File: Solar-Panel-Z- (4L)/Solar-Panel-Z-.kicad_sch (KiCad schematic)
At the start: 80 parts, among them J1 FTS-105-01-L-DV-A, J2 U.FL-R-SMT-1, Q1 BSS138DWQ-7, Q2 MBT2222ADW1T1, Q3 BSS138DWQ-7, Q4 MBT2222ADW1T1, Q5 IRLML2803, U1 BQ25570RGRR, U2 TSL2561, U3 ATB2012-50011-T000, U4 NDS8434

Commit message: Changed design to TSL2691 and IRF7404 on Z- (4L)
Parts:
- removed R1, R2: 0, Resistor_SMD:R_0402_1005Metric, symbol Device:R_US
- removed U2: TSL2561, solarpanels:TSL2561, symbol solarpanels:symbols_TSL2561
- removed U4: NDS8434, solarpanels:NDS8434, symbol solarpanels:symbols_NDS8434
- added U2: TSL2591, solarpanels:TSL2591, symbol solarpanels:symbols_TSL2591
- added U4: IRF7404, Package_SO:SOIC-8_3.9x4.9mm_P1.27mm, symbol Transistor_FET:IRF7404
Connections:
- net +3V3: now also U2.5 (VDD)
- net BATT_P: now also U4.1 (S), U4.2 (S), U4.3 (S)
- net GND: now also U2.3 (GND)
- net SCL_LS: now also U2.1 (SCL)
- net SDA_LS: now also U2.6 (SDA)
- net VBURN: now also U4.5 (D), U4.6 (D), U4.7 (D), U4.8 (D)
- net at R10.2, R5.2, R7.2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: now also R5.1, R6.2, U1.7 (VBAT_OV)
- net at Q5.3 (D), R33.1: now also U4.4 (G)
- no-connect marks 1 -> 2
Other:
- moved on the sheet: C1, C2, C3, C6, D1, D5, H1, H2, H3, H4, H5, H6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

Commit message: Changed TSL2591 to BH1750
All boards (4L) except -Y
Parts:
- removed U2: TSL2591, solarpanels:TSL2591, symbol solarpanels:symbols_TSL2591
- added R1, R2: 0, Resistor_SMD:R_0402_1005Metric, symbol Device:R_US
- added U2: BH1750FVI-TR, WSOF6, symbol solarpanels:BH1750FVI-TR
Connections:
- net +3V3: now also R1.2, U2.1 (VCC)
- net GND: now also R2.1, U2.3 (GND)
- net SCL_LS: now also U2.6 (SCL)
- net SDA_LS: now also U2.4 (SDA)
- new net: R1.1, R2.2, U2.2 (ADDR)
- no-connect marks 2 -> 1
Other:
- moved on the sheet: C1

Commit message: Updated light sensor to OPT 3001, Updated solar diodes.
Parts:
- removed C12, C13: 10nF, Capacitor_SMD:C_0603_1608Metric, symbol Device:C
- removed D5: MSS1P4-M3_89A, solarpanels:MICROSMP, symbol Device:D_Schottky
- removed Q1, Q3: BSS138DWQ-7, Package_TO_SOT_SMD:SOT-363_SC-70-6, symbol mainboard:BSS138DWQ-7
- removed Q2, Q4: MBT2222ADW1T1, Package_TO_SOT_SMD:SOT-363_SC-70-6, symbol Transistor_BJT:MBT2222ADW1T1
- removed R19, R20: DNI, Resistor_SMD:R_0603_1608Metric, symbol Device:R_US
- removed R21, R26: 680, Resistor_SMD:R_0603_1608Metric, symbol Device:R_US
- removed R22, R27: 100K, Resistor_SMD:R_0603_1608Metric, symbol Device:R_US
- removed R23, R24, R28, R29: 10K, Resistor_SMD:R_0603_1608Metric, symbol Device:R_US
- removed R25, R30: 200K, Resistor_SMD:R_0603_1608Metric, symbol Device:R_US
- removed U2: BH1750FVI-TR, WSOF6, symbol solarpanels:BH1750FVI-TR
- added R35: 1R, Resistor_SMD:R_1206_3216Metric, symbol Device:R_US
- added U2: OPT3001, solarpanels:OPT3001, symbol solarpanels:OPT3001
- added U4: MAX40200AUK, Package_TO_SOT_SMD:SOT-23-5, symbol Analog_Switch:MAX40200AUK
- D2, D3, D4: value MSS1P4-M3_89A -> DFLS130L-7; footprint solarpanels:MICROSMP -> Diode_SMD:D_PowerDI-123; Allied Price/Stock https://www.alliedelec.com/general-semiconductor-vishay-mss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 -> (none); Allied_Number 70217632 -> (none); Manufacturer_Name Vishay -> (none); Manufacturer_Part_Number MSS1P4-M3/89A -> (none); Mouser Part Number 625-MSS1P4-M3 -> (none); Mouser Price/Stock https://www.mouser.com/Search/Refine.aspx?Keyword=625-MSS1P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 -> (none); RS Part Number 7103068P -> (none); RS Price/Stock http://uk.rs-online.com/web/p/products/7103068P -> (none)
- J1: value FTS-105-01-L-DV-A -> FTS-105-01-X-DV-A
- J2: footprint solarpanels:U.FL-R-SMT-1 -> mainboard:U.FL-R-SMT-1; symbol solarpanels:U.FL-R-SMT-1 -> mainboard:U.FL-R-SMT-1
- JP1: value Jumper -> BurnWire 1
- JP2: value Jumper -> BurnWire 2
- R1, R12, R13, R16, R17, R18, R2, R3, R4: value 0 -> 0R
- R14, R15: value DNI -> DNI (0R)
- renumbered U4 to Q6, R31 to R32, R32 to R33, R33 to R34
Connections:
- net +3V3: now also U2.1 (VDD), U4.5 (OUT); no longer D2.1 (K)
- net GND: now also R35.2, U2.3 (GND), U2.7 (GND), U4.2 (GND); no longer JP1.2, JP2.2
- net SCL_LS: now also U2.4 (SCL)
- net SDA_LS: now also U2.6 (SDA)
- net VBURN: no longer JP2.1
- net VSOLAR: now also D2.1 (K)
- net VSOLAR_FULL: now also D2.2 (A)
- net at R10.2, R5.2, R7.2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: no longer R5.1, R6.2, U1.7 (VBAT_OV)
- net at R1.1, R2.2: now also U2.2 (ADDR)
- net at C10.1, C8.1, L2.2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: now also U4.1 (VDD), U4.3 (EN); no longer D2.2 (A)
- new net: R5.1, R6.2, U1.7 (VBAT_OV)
- new net: JP2.2, R35.1
- new net: JP1.2, JP2.1
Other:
- added sheet Bus Protection (BusProtection.kicad_sch)
- note added: "Antennas"
- note added: "Populate R1 for I2C addr 0x45, OR Populate R2 for I2C addr 0x44"
- note added: "To Mainboard"
- note removed: "I2C Bus Protection - Light Sensor"
- note removed: "Test Points"
- moved on the sheet: C1, C11, C6, H1, H2, H3, H4, H5, H6, J2, JP1, JP2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

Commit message: B3/02 Updates
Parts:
- C1: value 1uF -> 0.1uF
- H1, H2, H3, H4: footprint MountingHole:MountingHole_2.2mm_M2_DIN965_Pad -> solarpanels:MountingHole_2.2mm_M2_DIN965_Pad_TopBottom; now left out of the parts list
- H5, H6, TP1, TP2, TP3, TP4: now left out of the parts list
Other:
- moved on the sheet: C1, R1, R2, U2

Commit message: Minor Fixes
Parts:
- JP1: value BurnWire 1 -> BurnWire
- JP2: value BurnWire 2 -> BurnWire
- renumbered U3 to BA1, R32 to R31, R33 to R32, R34 to R33, R35 to R34, U4 to U3
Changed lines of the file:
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@@
   (symbol (lib_id "Device:R_US") (at 256.413 106.045 0) (unit 1)
     (in_bom yes) (on_board yes) (dnp no)
-    (property "Reference" "R32" (at 261.366 105.029 0)
+    (property "Reference" "R31" (at 261.366 105.029 0)
       (effects (font (size 1.2 1.2)) (justify right))
     )
@@
       (project "Solar-Panel-Z-"
         (path "/b5352a33-563a-4ffe-a231-2e68fb54afa3"
-          (reference "R32") (unit 1)
+          (reference "R31") (unit 1)
         )
       )
@@
   (symbol (lib_id "Device:R_US") (at 321.564 115.062 90) (unit 1)
     (in_bom yes) (on_board yes) (dnp no)
-    (property "Reference" "R35" (at 321.564 118.872 90)
+    (property "Reference" "R34" (at 321.564 118.872 90)
       (effects (font (size 1.2 1.2)))
     )
@@
       (project "Solar-Panel-Z-"
         (path "/b5352a33-563a-4ffe-a231-2e68fb54afa3"
-          (reference "R35") (unit 1)
+          (reference "R34") (unit 1)
         )
       )
@@
   (symbol (lib_id "solarpanels:ATB2012") (at 211.328 175.26 0) (unit 1)
     (in_bom yes) (on_board yes) (dnp no)
-    (property "Reference" "U3" (at 211.328 164.465 0)
+    (property "Reference" "BA1" (at 211.328 164.465 0)
       (effects (font (size 1.27 1.27)))
     )
@@
       (project "Solar-Panel-Z-"
         (path "/b5352a33-563a-4ffe-a231-2e68fb54afa3"
-          (reference "U3") (unit 1)
+          (reference "BA1") (unit 1)
         )
       )
@@
   (symbol (lib_id "Device:R_US") (at 261.493 100.965 270) (unit 1)
     (in_bom yes) (on_board yes) (dnp no)
-    (property "Reference" "R33" (at 261.493 97.155 90)
+    (property "Reference" "R32" (at 261.493 97.155 90)
       (effects (font (size 1.2 1.2)))
     )
@@
       (project "Solar-Panel-Z-"
         (path "/b5352a33-563a-4ffe-a231-2e68fb54afa3"
-          (reference "R33") (unit 1)
+          (reference "R32") (unit 1)
         )
       )
@@
       (effects (font (size 1.27 1.27)) (justify left))
     )
-    (property "Value" "BurnWire 1" (at 310.515 100.965 0)
+    (property "Value" "BurnWire" (at 310.515 101.981 0)
       (effects (font (size 1.27 1.27)) (justify left))
     )
@@
   )
   (symbol (lib_id "Analog_Switch:MAX40200AUK") (at 197.993 71.12 0) (unit 1)
-    (in_bom yes) (on_board yes) (dnp no) (fields_autoplaced)
-    (property "Reference" "U4" (at 197.993 62.103 0)
+    (in_bom yes) (on_board yes) (dnp no)
+    (property "Reference" "U3" (at 197.993 62.611 0)
       (effects (font (size 1.27 1.27)))
     )
@@
       (project "Solar-Panel-Z-"
         (path "/b5352a33-563a-4ffe-a231-2e68fb54afa3"
-          (reference "U4") (unit 1)
+          (reference "U3") (unit 1)
         )
       )
@@
       (effects (font (size 1.27 1.27)) (justify left))
     )
-    (property "Value" "BurnWire 2" (at 323.85 100.965 0)
+    (property "Value" "BurnWire" (at 323.85 101.981 0)
       (effects (font (size 1.27 1.27)) (justify left))
     )
@@
   (symbol (lib_id "Device:R_US") (at 275.717 104.775 180) (unit 1)
     (in_bom yes) (on_board yes) (dnp no)
-    (property "Reference" "R34" (at 277.241 104.013 0)
+    (property "Reference" "R33" (at 277.241 104.013 0)
       (effects (font (size 1.2 1.2)) (justify right))
     )
@@
       (project "Solar-Panel-Z-"
         (path "/b5352a33-563a-4ffe-a231-2e68fb54afa3"
-          (reference "R34") (unit 1)
-        )
-      )
+          (reference "R33") (unit 1)
+        )
+      )

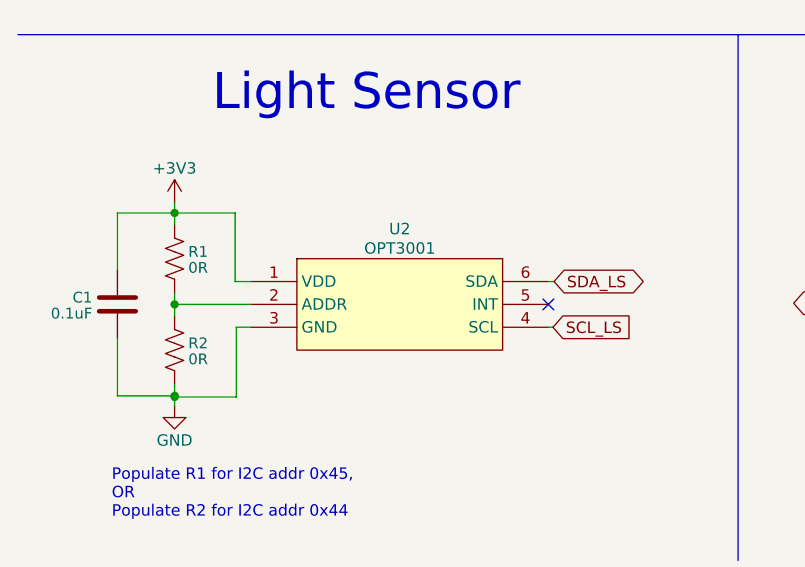
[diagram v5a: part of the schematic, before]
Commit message: Updated Sun Sensor to OPT4001
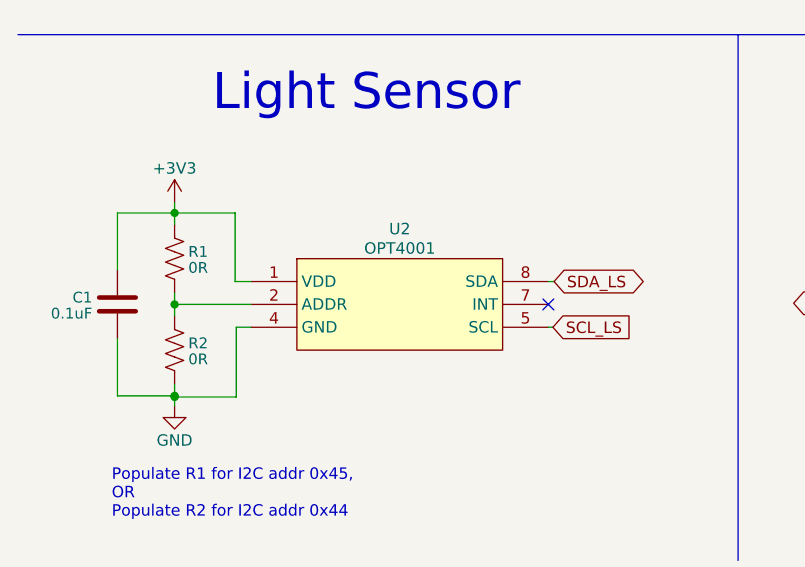
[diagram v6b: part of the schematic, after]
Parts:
- U2: value OPT3001 -> OPT4001; footprint solarpanels:OPT3001 -> Package_TO_SOT_SMD:SOT-583-8; symbol solarpanels:OPT3001 -> solarpanels:OPT4001
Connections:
- net GND: now also U2.4 (GND); no longer U2.3 (GND), U2.7 (GND)
- net SCL_LS: now also U2.5 (SCL); no longer U2.4 (SCL)
- net SDA_LS: now also U2.8 (SDA); no longer U2.6 (SDA)
- new net: U2.3 (NC), U2.6 (NC)
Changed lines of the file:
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@@
     )
   )
-  (symbol (lib_id "solarpanels:OPT3001") (at 53.848 176.022 0) (unit 1)
+  (symbol (lib_id "solarpanels:OPT4001") (at 53.848 176.022 0) (unit 1)
     (in_bom yes) (on_board yes) (dnp no)
     (property "Reference" "U2" (at 53.848 167.64 0)
       (effects (font (size 1.27 1.27)))
     )
-    (property "Value" "OPT3001" (at 53.848 169.799 0)
+    (property "Value" "OPT4001" (at 53.848 169.799 0)
       (effects (font (size 1.27 1.27)))
     )
-    (property "Footprint" "solarpanels:OPT3001" (at 53.848 182.372 0)
+    (property "Footprint" "Package_TO_SOT_SMD:SOT-583-8" (at 53.848 182.372 0)
       (effects (font (size 1.27 1.27)) hide)
     )
@@
     (pin "6")
     (pin "7")
+    (pin "8")
     (instances
       (project "Solar-Panel-Z-"
